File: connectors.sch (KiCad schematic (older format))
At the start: 4 parts, among them J1 Conn_01x04, J2 Conn_01x09, J3 Conn_02x03_Odd_Even, J4 Conn_01x04

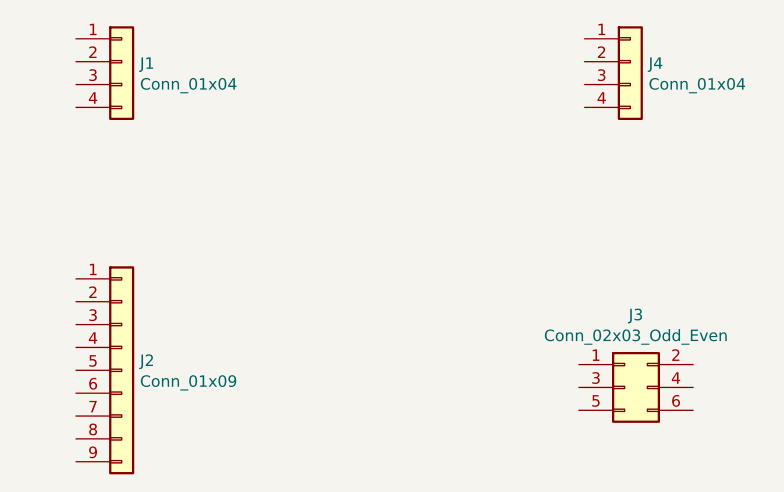
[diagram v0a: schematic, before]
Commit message: [eeshema] assign values, connect symbols
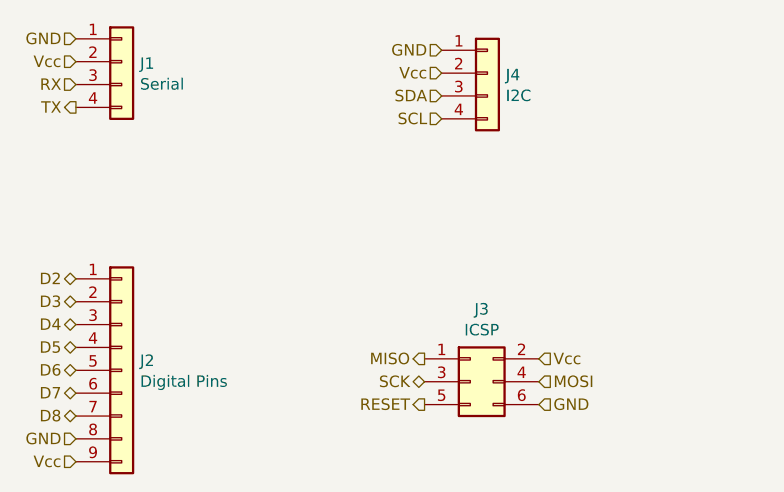
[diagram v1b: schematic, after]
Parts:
- J1: value Conn_01x04 -> Serial
- J2: value Conn_01x09 -> Digital Pins
- J3: value Conn_02x03_Odd_Even -> ICSP
- J4: value Conn_01x04 -> I2C
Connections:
- net D2: now reaches J2.1 (Pin_1)
- net D3: now reaches J2.2 (Pin_2)
- net D4: now reaches J2.3 (Pin_3)
- net D5: now reaches J2.4 (Pin_4)
- net D6: now reaches J2.5 (Pin_5)
- net D7: now reaches J2.6 (Pin_6)
- net D8: now reaches J2.7 (Pin_7)
- net GND: now reaches J2.8 (Pin_8)
- net GND: now also J1.1 (Pin_1), J3.6 (Pin_6), J4.1 (Pin_1)
- net Vcc: now reaches J2.9 (Pin_9)
- net Vcc: now also J1.2 (Pin_2), J3.2 (Pin_2), J4.2 (Pin_2)
- net SDA: now reaches J4.3 (Pin_3)
- net SCL: now reaches J4.4 (Pin_4)
- net MISO: now reaches J3.1 (Pin_1)
- net SCK: now reaches J3.3 (Pin_3)
- net MOSI: now reaches J3.4 (Pin_4)
- net RESET: now reaches J3.5 (Pin_5)
- net RX: now reaches J1.3 (Pin_3)
- net TX: now reaches J1.4 (Pin_4)
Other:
- moved on the sheet: J3, J4
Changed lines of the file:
@@
 P 3950 3500
 F 0 "J2" H 4030 3542 50  0000 L CNN
-F 1 "Conn_01x09" H 4030 3451 50  0000 L CNN
+F 1 "Digital Pins" H 4030 3451 50  0000 L CNN
 F 2 "Connector_PinHeader_2.54mm:PinHeader_1x09_P2.54mm_Vertical" H 3950 3500 50  0001 C CNN
 F 3 "~" H 3950 3500 50  0001 C CNN
@@
 L Connector_Generic:Conn_01x04 J4
 U 1 1 5EE5A90B
-P 6175 2150
-F 0 "J4" H 6255 2142 50  0000 L CNN
-F 1 "Conn_01x04" H 6255 2051 50  0000 L CNN
-F 2 "Connector_PinHeader_2.54mm:PinHeader_1x04_P2.54mm_Vertical" H 6175 2150 50  0001 C CNN
-F 3 "~" H 6175 2150 50  0001 C CNN
-	1    6175 2150
+P 5550 2200
+F 0 "J4" H 5630 2192 50  0000 L CNN
+F 1 "I2C" H 5630 2101 50  0000 L CNN
+F 2 "Connector_PinHeader_2.54mm:PinHeader_1x04_P2.54mm_Vertical" H 5550 2200 50  0001 C CNN
+F 3 "~" H 5550 2200 50  0001 C CNN
+	1    5550 2200
 	1    0    0    -1
 $EndComp
@@
 L Connector_Generic:Conn_02x03_Odd_Even J3
 U 1 1 5EE5ADAE
-P 6150 3575
-F 0 "J3" H 6200 3892 50  0000 C CNN
-F 1 "Conn_02x03_Odd_Even" H 6200 3801 50  0000 C CNN
-F 2 "Connector_PinHeader_2.54mm:PinHeader_2x03_P2.54mm_Vertical" H 6150 3575 50  0001 C CNN
-F 3 "~" H 6150 3575 50  0001 C CNN
-	1    6150 3575
+P 5475 3550
+F 0 "J3" H 5525 3867 50  0000 C CNN
+F 1 "ICSP" H 5525 3776 50  0000 C CNN
+F 2 "Connector_PinHeader_2.54mm:PinHeader_2x03_P2.54mm_Vertical" H 5475 3550 50  0001 C CNN
+F 3 "~" H 5475 3550 50  0001 C CNN
+	1    5475 3550
 	1    0    0    -1
 $EndComp
@@
 P 3950 2150
 F 0 "J1" H 4030 2142 50  0000 L CNN
-F 1 "Conn_01x04" H 4030 2051 50  0000 L CNN
+F 1 "Serial" H 4030 2051 50  0000 L CNN
 F 2 "Connector_PinHeader_2.54mm:PinHeader_1x04_P2.54mm_Vertical" H 3950 2150 50  0001 C CNN
 F 3 "~" H 3950 2150 50  0001 C CNN
@@
 	1    0    0    -1
 $EndComp
+Text HLabel 5275 3450 0    50   Output ~ 0
+MISO
+Text HLabel 5275 3550 0    50   BiDi ~ 0
+SCK
+Text HLabel 5775 3450 2    50   Input ~ 0
+Vcc
+Text HLabel 5775 3550 2    50   Input ~ 0
+MOSI
+Text HLabel 5275 3650 0    50   Output ~ 0
+RESET
+Text HLabel 5775 3650 2    50   Input ~ 0
+GND
+Text HLabel 3750 2050 0    50   Input ~ 0
+GND
+Text HLabel 3750 2250 0    50   Input ~ 0
+RX
+Text HLabel 3750 2350 0    50   Output ~ 0
+TX
+Text HLabel 3750 2150 0    50   Input ~ 0
+Vcc
+Text HLabel 5350 2100 0    50   Input ~ 0
+GND
+Text HLabel 5350 2200 0    50   Input ~ 0
+Vcc
+Text HLabel 5350 2300 0    50   Input ~ 0
+SDA
+Text HLabel 5350 2400 0    50   Input ~ 0
+SCL
+Text HLabel 3750 3100 0    50   BiDi ~ 0
+D2
+Text HLabel 3750 3200 0    50   BiDi ~ 0
+D3
+Text HLabel 3750 3300 0    50   BiDi ~ 0
+D4
+Text HLabel 3750 3400 0    50   BiDi ~ 0
+D5
+Text HLabel 3750 3500 0    50   BiDi ~ 0
+D6
+Text HLabel 3750 3600 0    50   BiDi ~ 0
+D7
+Text HLabel 3750 3700 0    50   BiDi ~ 0
+D8
+Text HLabel 3750 3900 0    50   Input ~ 0
+Vcc
+Text HLabel 3750 3800 0    50   Input ~ 0
+GND
 $EndSCHEMATC
